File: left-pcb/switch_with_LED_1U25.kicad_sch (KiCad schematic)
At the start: 3 parts, among them SW7 SW_SPST

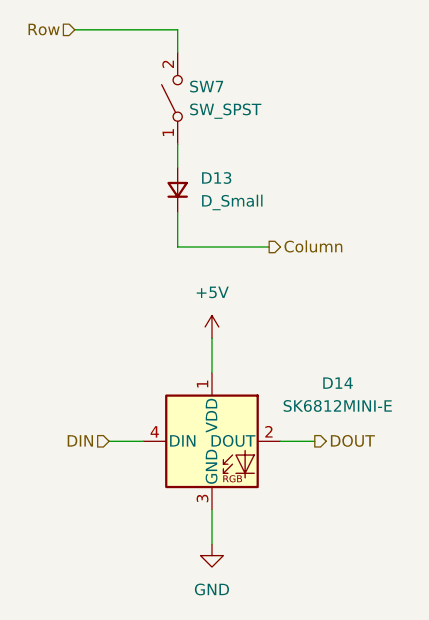
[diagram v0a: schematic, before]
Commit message: Initial modifications to reduce fab cost and add caps
Removing 1 row and column of keys, and majorly changing layout

Routing still in progress
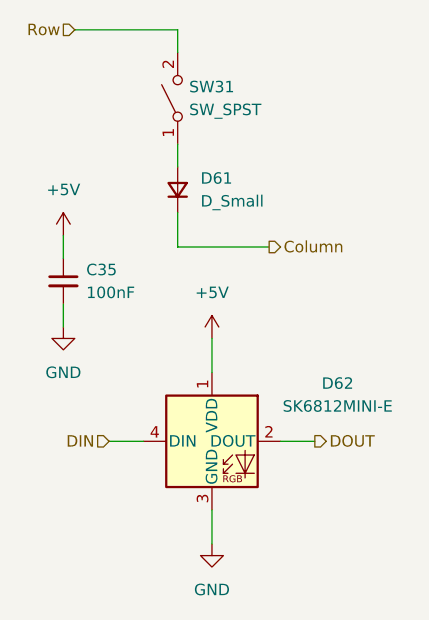
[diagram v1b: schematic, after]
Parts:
- removed D13: D_Small, Diode_SMD:D_SOD-123, symbol Device:D_Small
- removed D14: SK6812MINI-E, SW-Adafruit:LED_SK6812MINI-E_REVERSE_MOUNT_3.2x2.8mm_P1.09mm, symbol SW-Adafruit:SK6812MINI-E
- removed SW7: SW_SPST, PCM_Switch_Keyboard_Hotswap_Kailh:SW_Hotswap_Kailh_MX_1.25u, symbol Switch:SW_SPST
- added C35: 100nF, Capacitor_SMD:C_1206_3216Metric_Pad1.33x1.80mm_HandSolder, symbol Device:C_Small
- added D61: D_Small, Diode_SMD:D_SOD-123, symbol Device:D_Small
- added D62: SK6812MINI-E, SW-Adafruit:LED_SK6812MINI-E_REVERSE_MOUNT_3.2x2.8mm_P1.09mm, symbol SW-Adafruit:SK6812MINI-E
- added SW31: SW_SPST, PCM_Switch_Keyboard_Hotswap_Kailh:SW_Hotswap_Kailh_MX_1.25u, symbol Switch:SW_SPST
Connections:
- net +5V: now also C35.1, D62.1 (VDD)
- net Column: now also D61.1 (K)
- net DIN: now also D62.4 (DIN)
- net DOUT: now also D62.2 (DOUT)
- net GND: now also C35.2, D62.3 (GND)
- net Row: now also SW31.2 (B)
- new net: D61.2 (A), SW31.1 (A)

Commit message: Caps, shrunk board, added mounting holes
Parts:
- C35: footprint Capacitor_SMD:C_1206_3216Metric_Pad1.33x1.80mm_HandSolder -> Capacitor_SMD:C_0805_2012Metric_Pad1.18x1.45mm_HandSolder
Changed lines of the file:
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@@
 			)
 		)
-		(property "Footprint" "Capacitor_SMD:C_1206_3216Metric_Pad1.33x1.80mm_HandSolder"
+		(property "Footprint" "Capacitor_SMD:C_0805_2012Metric_Pad1.18x1.45mm_HandSolder"
 			(at 107.95 114.3 0)
 			(effects

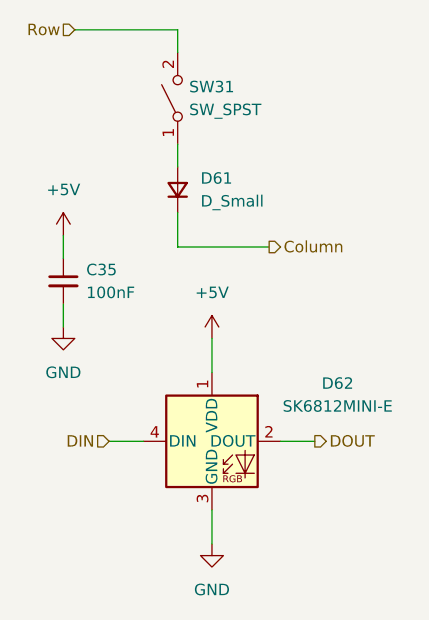
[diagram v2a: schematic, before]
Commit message: Adding values to Diodes and adding stabilizers to 2U switches
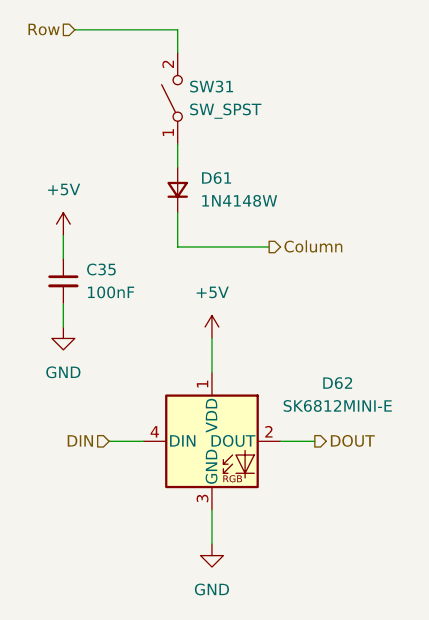
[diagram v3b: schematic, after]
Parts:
- D61: value D_Small -> 1N4148W
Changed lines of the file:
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@@
 			)
 		)
-		(property "Value" "D_Small"
+		(property "Value" "1N4148W"
 			(at 123.19 105.4099 90)
 			(effects

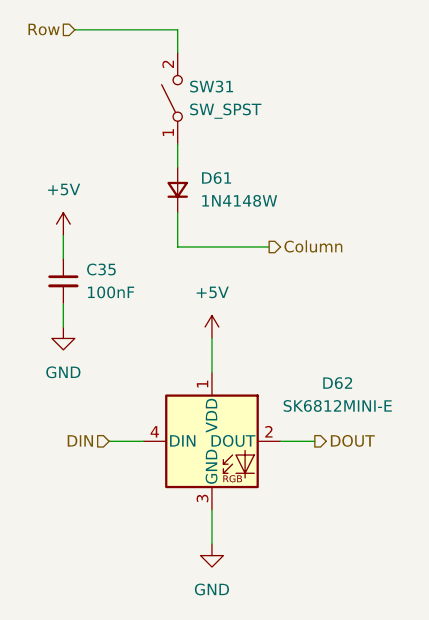
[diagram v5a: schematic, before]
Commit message: adding mounting hole in center for additional support, and cleaning up tracks/zones
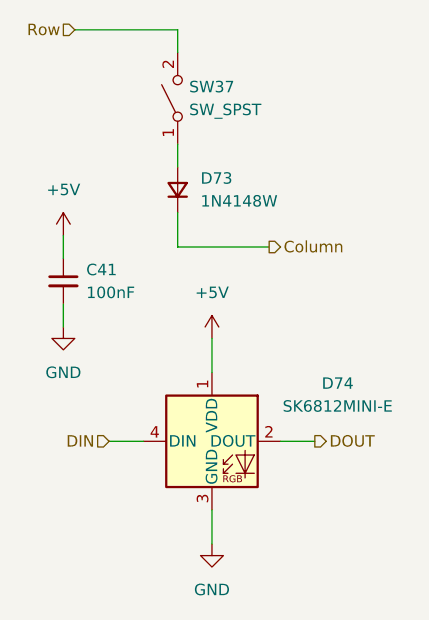
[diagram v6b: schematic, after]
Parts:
- renumbered C35 to C41, D61 to D73, D62 to D74, SW31 to SW37

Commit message: Boards were ordered
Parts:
- SW37: symbol Switch:SW_SPST -> SW-gElectroMech:SPST_MOM
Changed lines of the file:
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@@
 	)
 	(symbol
-		(lib_id "Switch:SW_SPST")
+		(lib_id "SW-gElectroMech:SPST_MOM")
 		(at 120.65 93.98 90)
 		(unit 1)
@@
 		)
 		(property "Datasheet" ""
-			(at 120.65 93.98 0)
+			(at 115.57 93.98 0)
 			(hide yes)
 			(show_name no)
@@
 			)
 		)
-		(property "Description" "Single Pole Single Throw (SPST) switch"
+		(property "Description" "Push button switch, generic, two pins"
 			(at 120.65 93.98 0)
 			(hide yes)
